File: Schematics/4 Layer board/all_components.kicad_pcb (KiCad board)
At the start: 4 copper layers, 131.5 x 122.5 mm, 78 parts, among them J2 Conn_01x01, J3 5V-Relay, J4 5V-Relay, J8 S08B-PUDSS-1LFSN, J9 3-pin-header, Q1 OPTOCOUPLER, Q2 OPTOCOUPLER, T1 PNP, T2 PNP, T3 PNP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

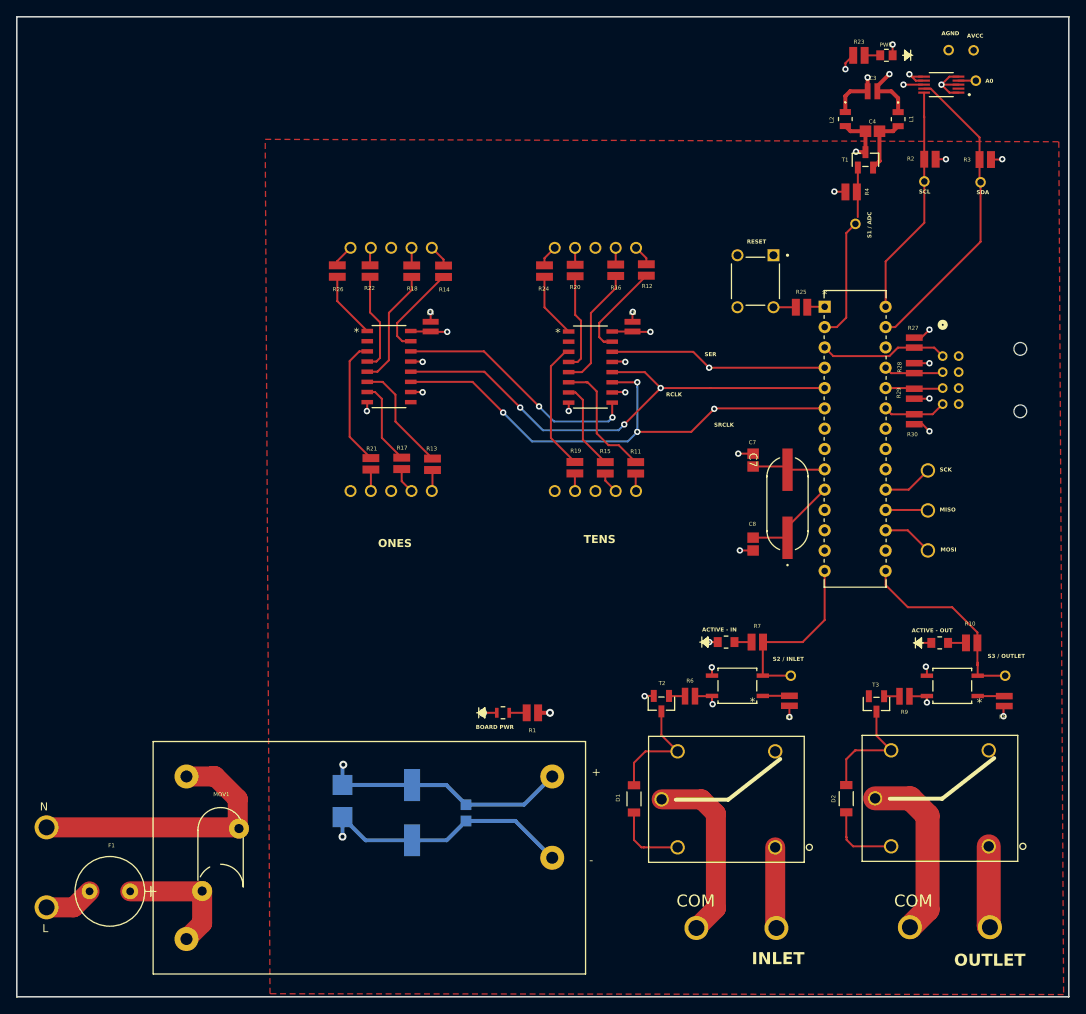
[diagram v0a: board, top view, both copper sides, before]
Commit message: updated board and kicad lib
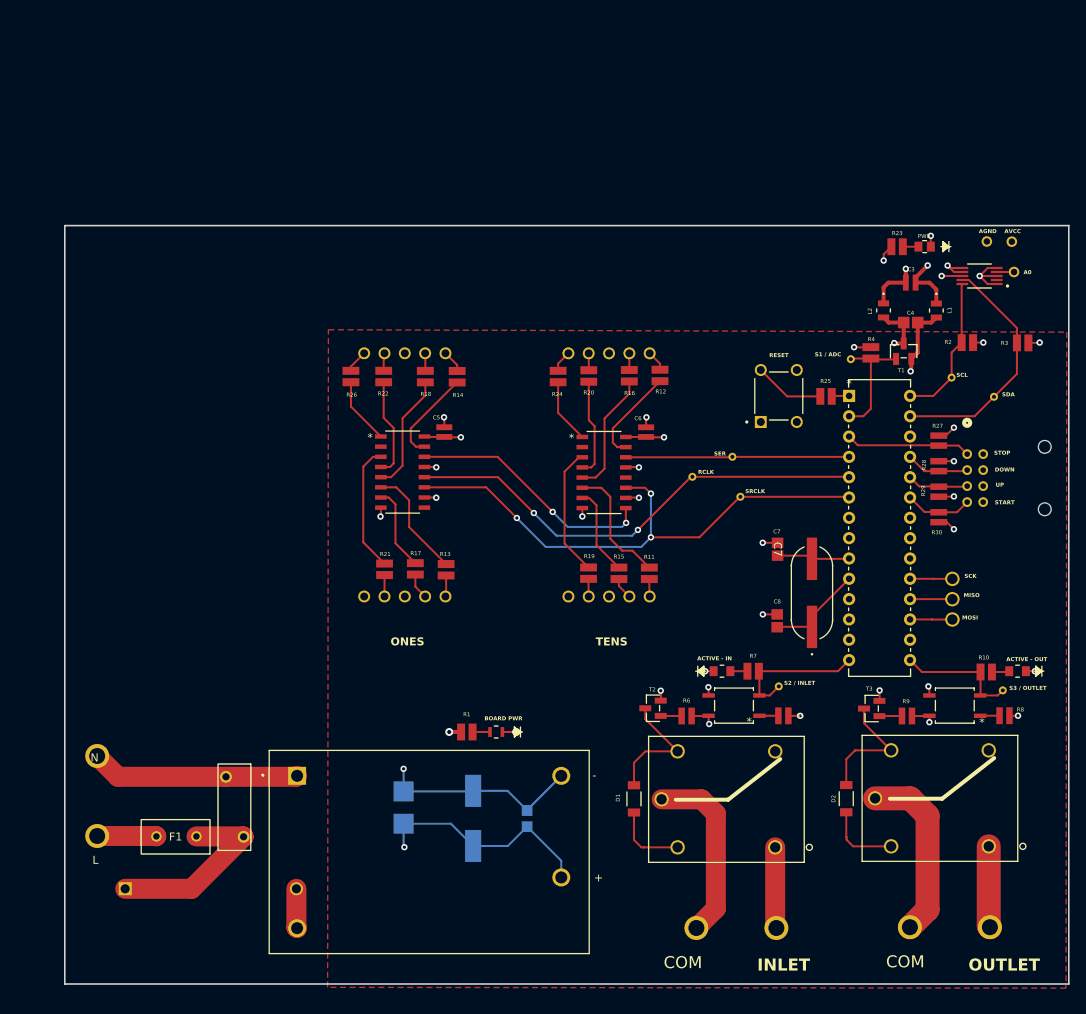
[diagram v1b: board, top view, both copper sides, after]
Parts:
- removed u1: AC-5VDC-Converter, pPSI:ac-dc converter
- added R31: 6.8ohm, pPSI:6.8ohm, B.Cu at (34.1, 153.5)
- added RCLK1: Conn_01x01, pPSI:1 pin header, F.Cu at (105.0, 102.0)
- added SERIAL1: Conn_01x01, pPSI:1 pin header, F.Cu at (110.0, 99.5)
- added SRCLK1: Conn_01x01, pPSI:1 pin header, F.Cu at (111.0, 104.5)
- added u3: AC-5VDC-Converter, pPSI:CONV_PSK-10D-5, F.Cu at (72.1, 148.9)
- F1: footprint pPSI:FUSE -> pPSI:Fuse
- MOV1: value 470V-Varistor -> ~; footprint pPSI:470V Varistor -> pPSI:350V_4.5kA MOV
- moved SDA1 26.9 mm to (142.7, 92.0)
- moved SCL1 24.8 mm to (137.4, 89.6)
- moved J2 24.4 mm to (145.2, 76.4)
- moved L1 24.4 mm to (135.5, 81.2)
- moved LED2 24.4 mm to (134.0, 73.2)
- moved AVCC1 24.4 mm to (144.9, 72.6)
- moved C3 24.4 mm to (132.3, 77.7)
- moved R23 24.4 mm to (130.6, 73.2)
- moved U2 24.4 mm to (140.9, 76.9)
- moved AGND1 24.4 mm to (141.8, 72.6)
- moved C4 24.4 mm to (132.3, 82.7)
- moved L2 24.4 mm to (128.9, 81.2)
- moved T1 24.4 mm to (131.4, 86.3)
- moved R2 23.4 mm to (139.4, 85.2)
- moved R3 23.4 mm to (146.3, 85.3)
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- renumbered 1 to 11
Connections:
- C1 pad 1: /GND -> /VCC
- C1 pad 2: /VCC -> /GND
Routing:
- net /SCL: track 29.0 -> 18.6 mm
- net /S3: track 24.8 -> 15.5 mm
- net /Neutral: track 35.3 -> 26.1 mm
- net /SDA: track 38.8 -> 30.6 mm
- net Net-(F1-Pad1): track 15.8 -> 23.4 mm
- net /GND: track 79.5 -> 72.2 mm
- net /S1: track 21.6 -> 15.0 mm
- net Net-(B1-Pad2): track 2.80 -> 8.81 mm
- net /RCLK: track 63.8 -> 58.9 mm, vias 3 -> 2
- net Net-(u3-AC_L): track 0.00 -> 4.96 mm
- net /S2: track 22.7 -> 17.8 mm
- net /SRCLK: track 65.9 -> 67.5 mm, vias 4 -> 3
- net Net-(D1-Pad2): track 14.9 -> 16.1 mm
- net /LIVE: track 6.25 -> 7.42 mm
- net /MOSI: track 6.33 -> 5.29 mm
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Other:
- board size 131.5 x 122.5 mm -> 125.5 x 94.8 mm
- board text added: "DOWN"
- board text added: "START"
- board text added: "STOP"
- board text added: "UP"

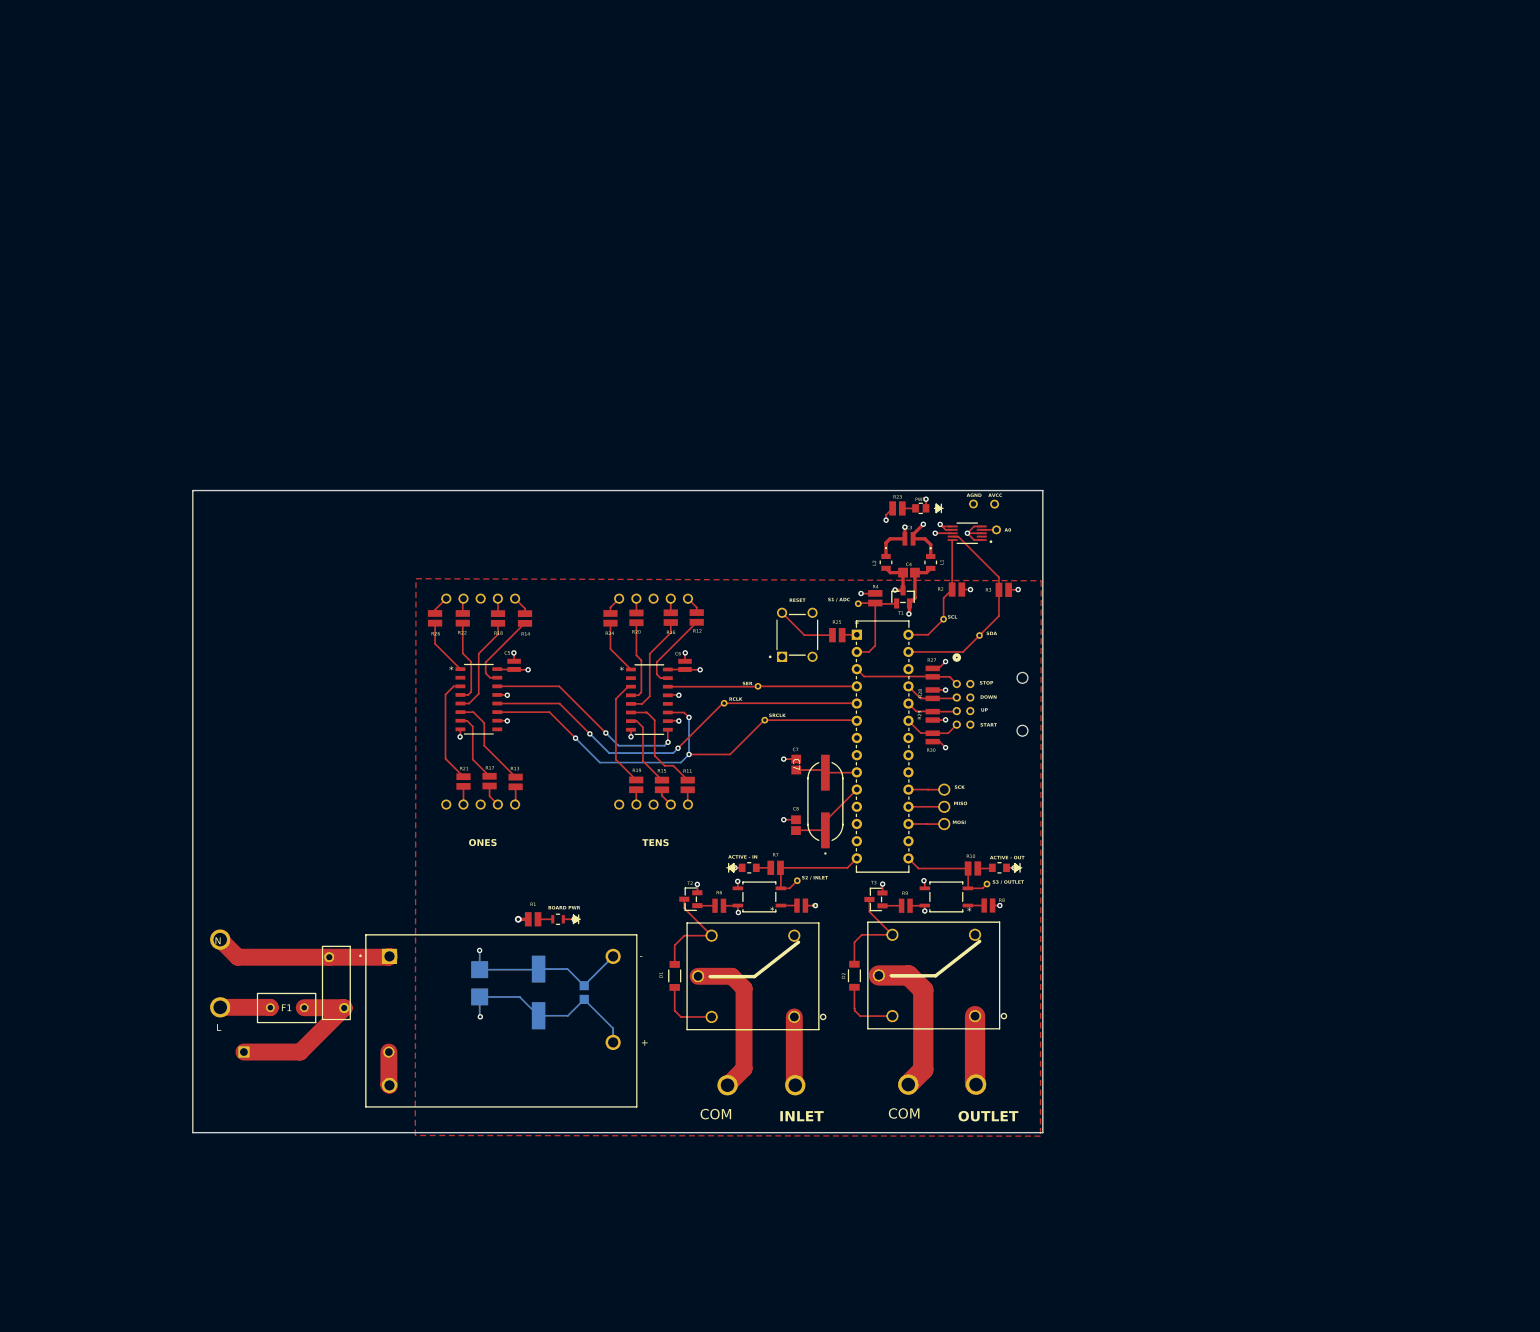
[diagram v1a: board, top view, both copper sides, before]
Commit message: updated kicad board and parts library
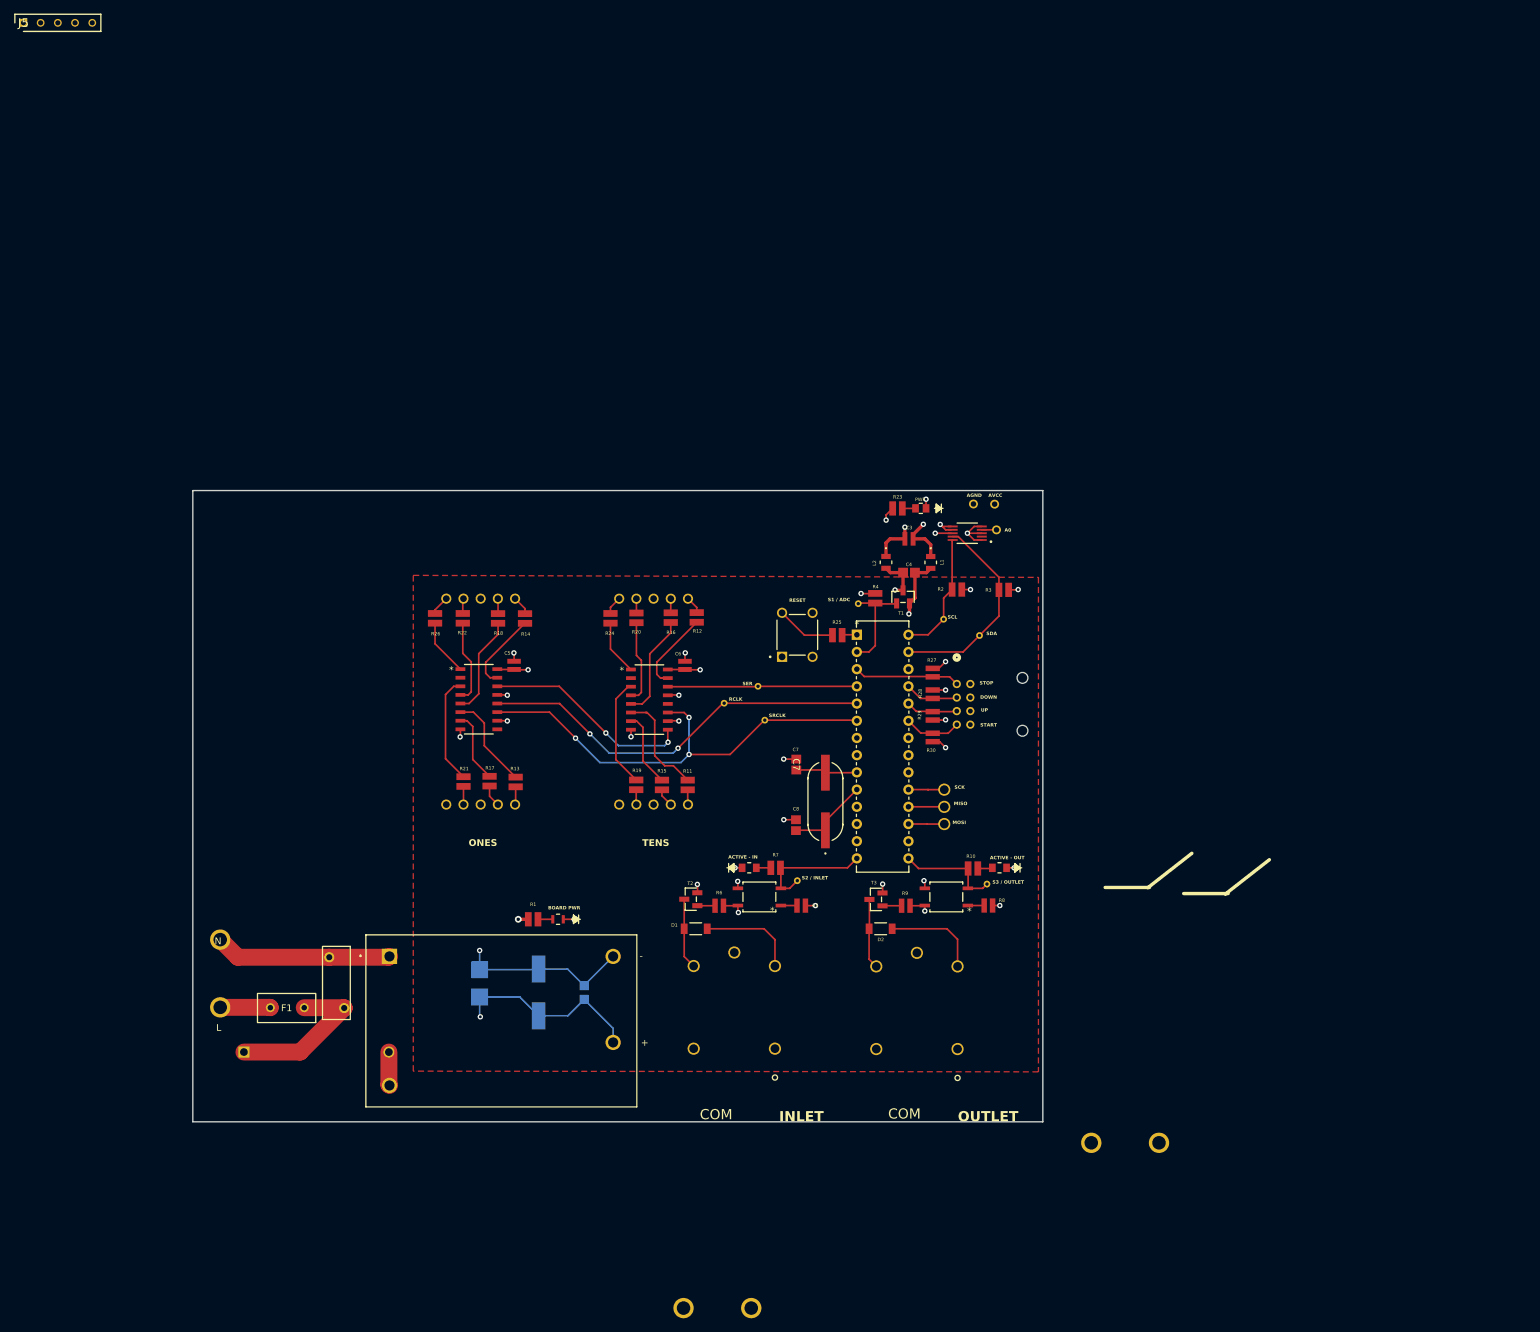
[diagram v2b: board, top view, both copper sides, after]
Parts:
- added J5: D01-9970542, pPSI:1x5 female header, F.Cu at (1.54, 1.54)
- J3, J4: moved to B.Cu
- moved J6 36.8 mm to (99.0, 191.3), turned to 0 degrees
- moved J7 19.1 mm to (159.2, 166.9), turned to 0 degrees
- moved D2 7.94 mm to (128.1, 135.3), turned to 180 degrees
- moved D1 7.62 mm to (100.8, 135.3), turned to 180 degrees
- moved J4 5.24 mm to (127.5, 140.9), turned to 90 degrees
- moved J3 5.21 mm to (100.5, 140.8), turned to 90 degrees
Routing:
- net /COM_INLET: track 22.8 -> 0.00 mm
- net /COM_OUTLET: track 22.3 -> 0.00 mm
- net /GND: track 72.2 -> 82.5 mm
- net /N/O_OUTLET: track 10.2 -> 0.00 mm
- net /N/O_INLET: track 10.1 -> 0.00 mm
- net Net-(D1-Pad2): track 16.1 -> 10.5 mm
- net Net-(D2-Pad2): track 15.9 -> 10.3 mm
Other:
- board size 125.5 x 94.8 mm -> 125.5 x 93.2 mm

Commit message: updated board for AC optimization
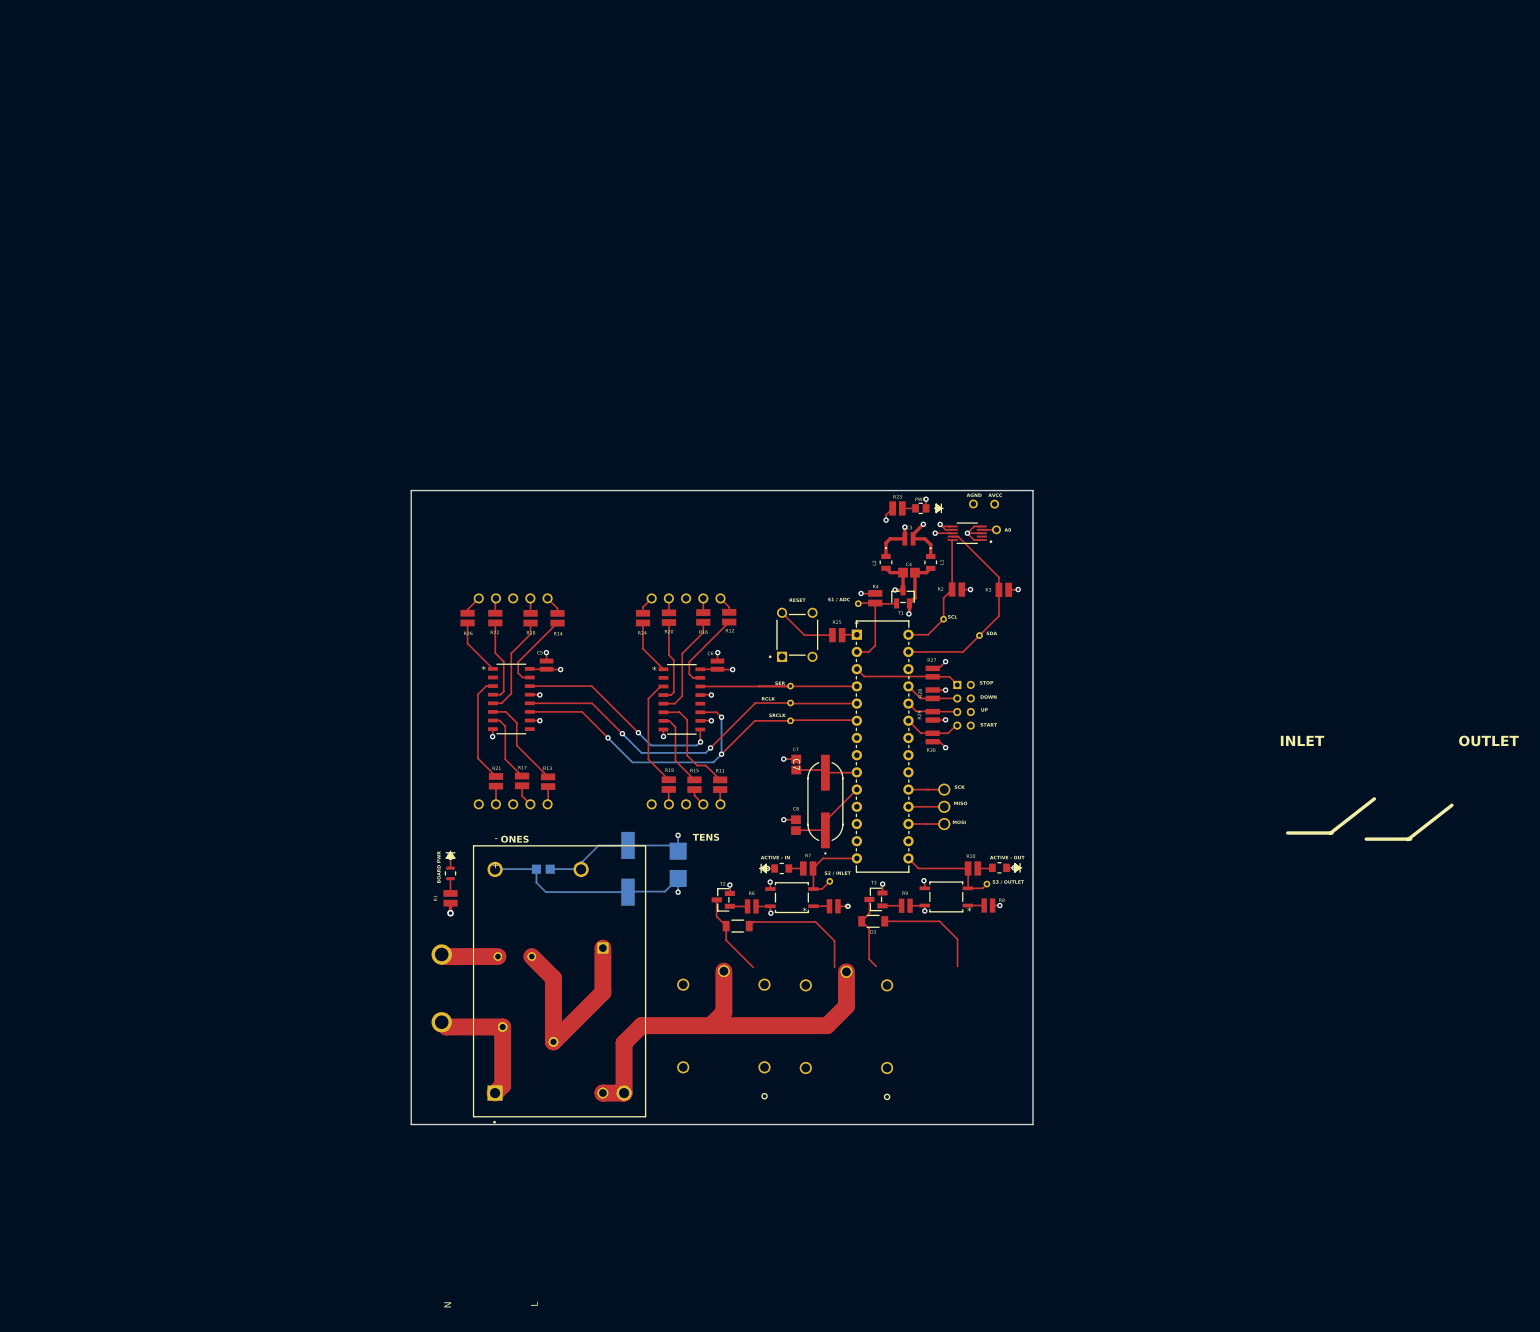
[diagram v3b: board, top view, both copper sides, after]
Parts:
- removed J6, J7: ~, pPSI:2 pin header
- removed J8: S08B-PUDSS-1LFSN, pPSI:2x4Connector
- F1, J1, MOV1: moved to B.Cu
- J5: value D01-9970542 -> S8B-PHDSS; footprint pPSI:1x5 female header -> pPSI:2x4 female connector; moved to B.Cu
- moved J5 169.0 mm to (139.4, 99.3), turned to -90 degrees
- moved R31 55.2 mm to (87.1, 138.1), turned to -90 degrees
- moved F1 34.4 mm to (76.6, 139.4)
- moved TVS1 34.1 mm to (98.2, 125.9), turned to -90 degrees
- moved J1 33.6 mm to (63.3, 139.1), turned to -90 degrees
- moved MOV1 27.6 mm to (72.3, 149.8), turned to 0 degrees
- moved C2 22.5 mm to (90.8, 126.4), turned to -90 degrees
- moved C1 19.2 mm to (78.3, 126.5), turned to 180 degrees
- moved LED1 17.3 mm to (64.6, 127.1), turned to -90 degrees
- moved R1 12.6 mm to (64.6, 130.8), turned to -90 degrees
- moved J4 10.8 mm to (117.1, 143.7)
- moved u3 10.4 mm to (80.7, 143.1), turned to 90 degrees
- moved RCLK1 9.80 mm to (114.8, 102.0)
- moved D1 6.21 mm to (107.0, 134.9)
- moved R7 4.80 mm to (117.4, 126.4)
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- renumbered active1 to A2, active2 to A3
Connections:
- J3 pad 5: /COM_INLET -> /LIVE
- J4 pad 5: /COM_OUTLET -> /LIVE
- J5 pad 1: /GND -> /STOP
- J5 pad 2: Net-(J5-Pad2) -> /GND
- J5 pad 3: /GND -> /DOWN
- J5 pad 4: Net-(J5-Pad4) -> /GND
- J5 pad 5: Net-(J5-Pad5) -> /UP
- R11 pad 2: Net-(J5-Pad5) -> Net-(R11-Pad2)
- R15 pad 2: Net-(J5-Pad4) -> Net-(R15-Pad2)
- R19 pad 2: Net-(J5-Pad2) -> Net-(R19-Pad2)
- R31 pad 2: Net-(u3-AC_L) -> /LIVE
- TENS1 pad 1: Net-(J5-Pad5) -> Net-(R11-Pad2)
- TENS1 pad 2: Net-(J5-Pad4) -> Net-(R15-Pad2)
- TENS1 pad 4: Net-(J5-Pad2) -> Net-(R19-Pad2)
- u3 pad 2: Net-(u3-AC_L) -> /LIVE
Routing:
- net /LIVE: track 7.42 -> 68.1 mm
- net /GND: track 82.5 -> 94.4 mm
- net Net-(F1-Pad1): track 23.4 -> 30.8 mm
- net /Neutral: track 26.1 -> 19.5 mm
- net /VCC: track 71.6 -> 65.6 mm
- net Net-(u3-AC_L): track 4.96 -> 0.00 mm
- net /S2: track 17.8 -> 13.0 mm
- net /SRCLK: track 67.5 -> 62.9 mm
- net /RCLK: track 58.9 -> 54.5 mm
- net Net-(J5-Pad4): track 2.73 -> 0.00 mm
- net Net-(R15-Pad2): track 0.00 -> 2.73 mm
- net Net-(R19-Pad2): track 0.00 -> 2.21 mm
- net Net-(J5-Pad2): track 2.21 -> 0.00 mm
- net Net-(J5-Pad5): track 2.20 -> 0.00 mm
- net Net-(R11-Pad2): track 0.00 -> 2.20 mm
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- removed copper zone on F.Cu, net (none)
- removed copper zone on In1.Cu, net /GND
- removed copper zone on In2.Cu, net /VCC
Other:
- board size 125.5 x 93.2 mm -> 91.8 x 93.6 mm
- board text removed: "COM"
